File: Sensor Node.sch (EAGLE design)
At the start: 31 parts, among them Q1 IRLML6402, U1 ATMEGA328P_TQFP, X16 16MHZ, X8 8MHZ

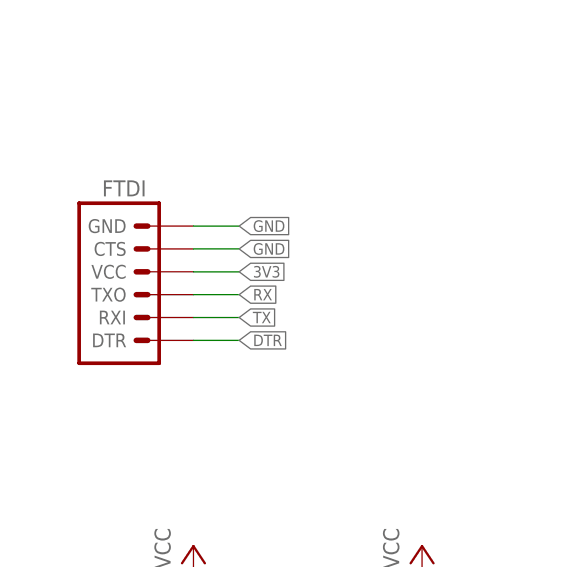
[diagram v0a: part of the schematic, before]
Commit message: Refactoring
Replace the FTDI pinheader
Remove unwanted text
Move and resize text
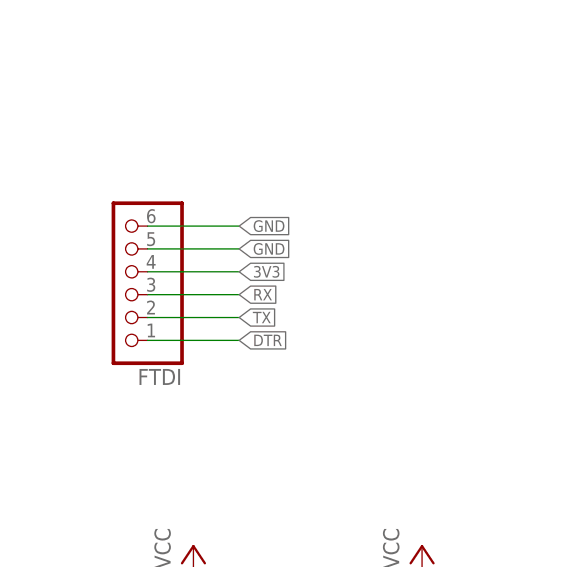
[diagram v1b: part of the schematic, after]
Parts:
- FTDI: device SparkFun-Connectors:ARDUINO_SERIAL_PROGRAMLOCK -> pinhead:PINHD-1X6
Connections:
- net 3V3: now also FTDI.4; no longer FTDI.VCC
- net DTR: now also FTDI.1; no longer FTDI.DTR
- net GND: now also FTDI.5, FTDI.6; no longer FTDI.CTS, FTDI.GND
- net RX: now also FTDI.3; no longer FTDI.TXO
- net TX: now also FTDI.2; no longer FTDI.RXI
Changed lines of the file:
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@@
 </classes>
 <parts>
-<part name="FTDI" library="SparkFun-Connectors" deviceset="ARDUINO_SERIAL_PROGRAM" device="LOCK"/>
 <part name="C2" library="rcl" deviceset="C-EU" device="C0402" value="100n"/>
 <part name="BATTERY" library="pinhead" deviceset="PINHD-1X2" device=""/>
@@
 <part name="GND6" library="supply1" deviceset="GND" device=""/>
 <part name="R3" library="rcl" deviceset="R-EU_" device="R0402" value="10k"/>
+<part name="FTDI" library="pinhead" deviceset="PINHD-1X6" device=""/>
 </parts>
 <sheets>
@@
 </plain>
 <instances>
-<instance part="FTDI" gate="G$1" x="0" y="109.22"/>
 <instance part="C2" gate="G$1" x="0" y="63.5" rot="R270"/>
 <instance part="BATTERY" gate="G$1" x="25.4" y="187.96" rot="R180"/>
@@
 <instance part="GND6" gate="1" x="50.8" y="160.02" smashed="yes"/>
 <instance part="R3" gate="G$1" x="50.8" y="170.18" rot="R90"/>
+<instance part="FTDI" gate="A" x="-2.54" y="111.76" rot="R180"/>
 </instances>
 <busses>
@@
 </segment>
 <segment>
-<pinref part="FTDI" gate="G$1" pin="GND"/>
-<wire x1="5.08" y1="116.84" x2="10.16" y2="116.84" width="0.1524" layer="91"/>
 <label x="10.16" y="116.84" size="1.27" layer="95" xref="yes"/>
-</segment>
-<segment>
-<pinref part="FTDI" gate="G$1" pin="CTS"/>
-<wire x1="5.08" y1="114.3" x2="10.16" y2="114.3" width="0.1524" layer="91"/>
+<pinref part="FTDI" gate="A" pin="6"/>
+<wire x1="10.16" y1="116.84" x2="0" y2="116.84" width="0.1524" layer="91"/>
+</segment>
+<segment>
 <label x="10.16" y="114.3" size="1.27" layer="95" xref="yes"/>
+<pinref part="FTDI" gate="A" pin="5"/>
+<wire x1="10.16" y1="114.3" x2="0" y2="114.3" width="0.1524" layer="91"/>
 </segment>
 <segment>
@@
 </segment>
 <segment>
-<pinref part="FTDI" gate="G$1" pin="TXO"/>
-<wire x1="5.08" y1="109.22" x2="10.16" y2="109.22" width="0.1524" layer="91"/>
 <label x="10.16" y="109.22" size="1.27" layer="95" xref="yes"/>
+<pinref part="FTDI" gate="A" pin="3"/>
+<wire x1="10.16" y1="109.22" x2="0" y2="109.22" width="0.1524" layer="91"/>
 </segment>
 </net>
@@
 </segment>
 <segment>
-<pinref part="FTDI" gate="G$1" pin="RXI"/>
-<wire x1="5.08" y1="106.68" x2="10.16" y2="106.68" width="0.1524" layer="91"/>
 <label x="10.16" y="106.68" size="1.27" layer="95" xref="yes"/>
+<pinref part="FTDI" gate="A" pin="2"/>
+<wire x1="10.16" y1="106.68" x2="0" y2="106.68" width="0.1524" layer="91"/>
 </segment>
 </net>
@@
 <net name="DTR" class="0">
 <segment>
-<pinref part="FTDI" gate="G$1" pin="DTR"/>
-<wire x1="5.08" y1="104.14" x2="10.16" y2="104.14" width="0.1524" layer="91"/>
 <label x="10.16" y="104.14" size="1.27" layer="95" xref="yes"/>
+<pinref part="FTDI" gate="A" pin="1"/>
+<wire x1="10.16" y1="104.14" x2="0" y2="104.14" width="0.1524" layer="91"/>
 </segment>
 <segment>
@@
 <net name="3V3" class="1">
 <segment>
-<pinref part="FTDI" gate="G$1" pin="VCC"/>
-<wire x1="5.08" y1="111.76" x2="10.16" y2="111.76" width="0.1524" layer="91"/>
 <label x="10.16" y="111.76" size="1.27" layer="95" xref="yes"/>
-</segment>
-<segment>
+<pinref part="FTDI" gate="A" pin="4"/>
+<wire x1="10.16" y1="111.76" x2="0" y2="111.76" width="0.1524" layer="91"/>
+</segment>
+<segment>
